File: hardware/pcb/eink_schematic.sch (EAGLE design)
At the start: 2 parts, among them U1 NUCLEUM

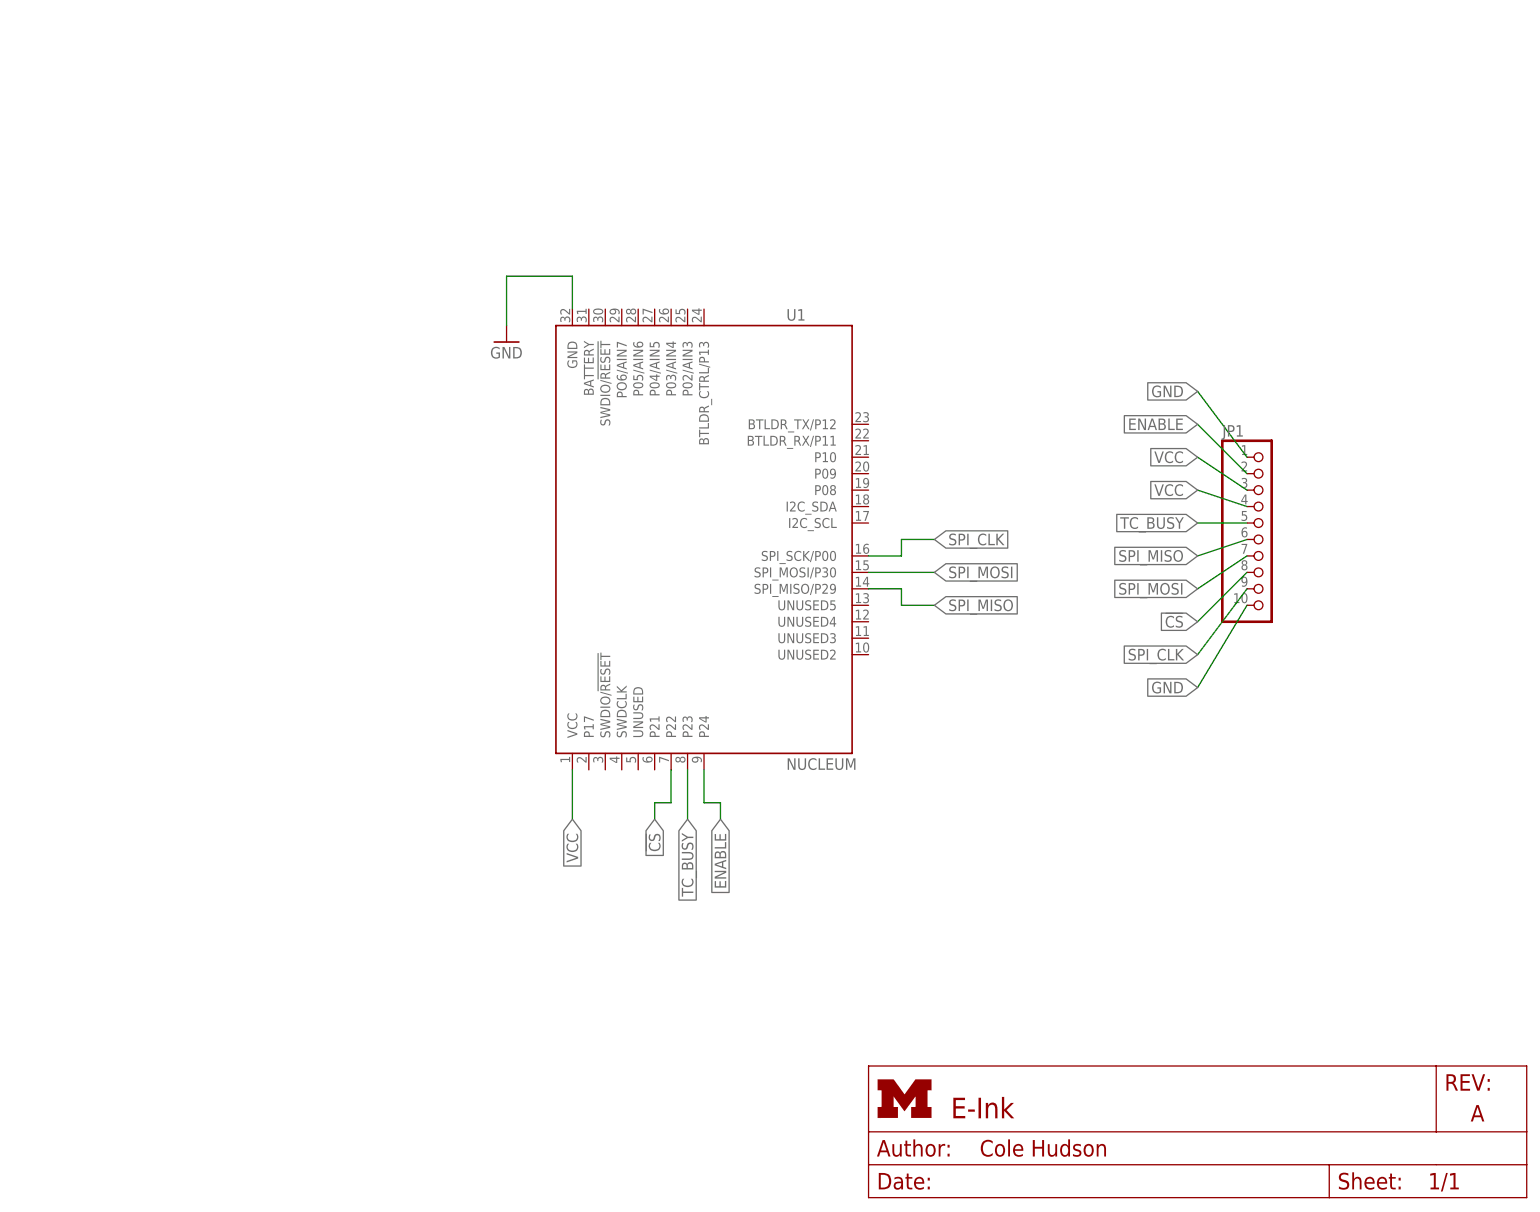
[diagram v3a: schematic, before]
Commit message: added buck/boost regulator to schematic
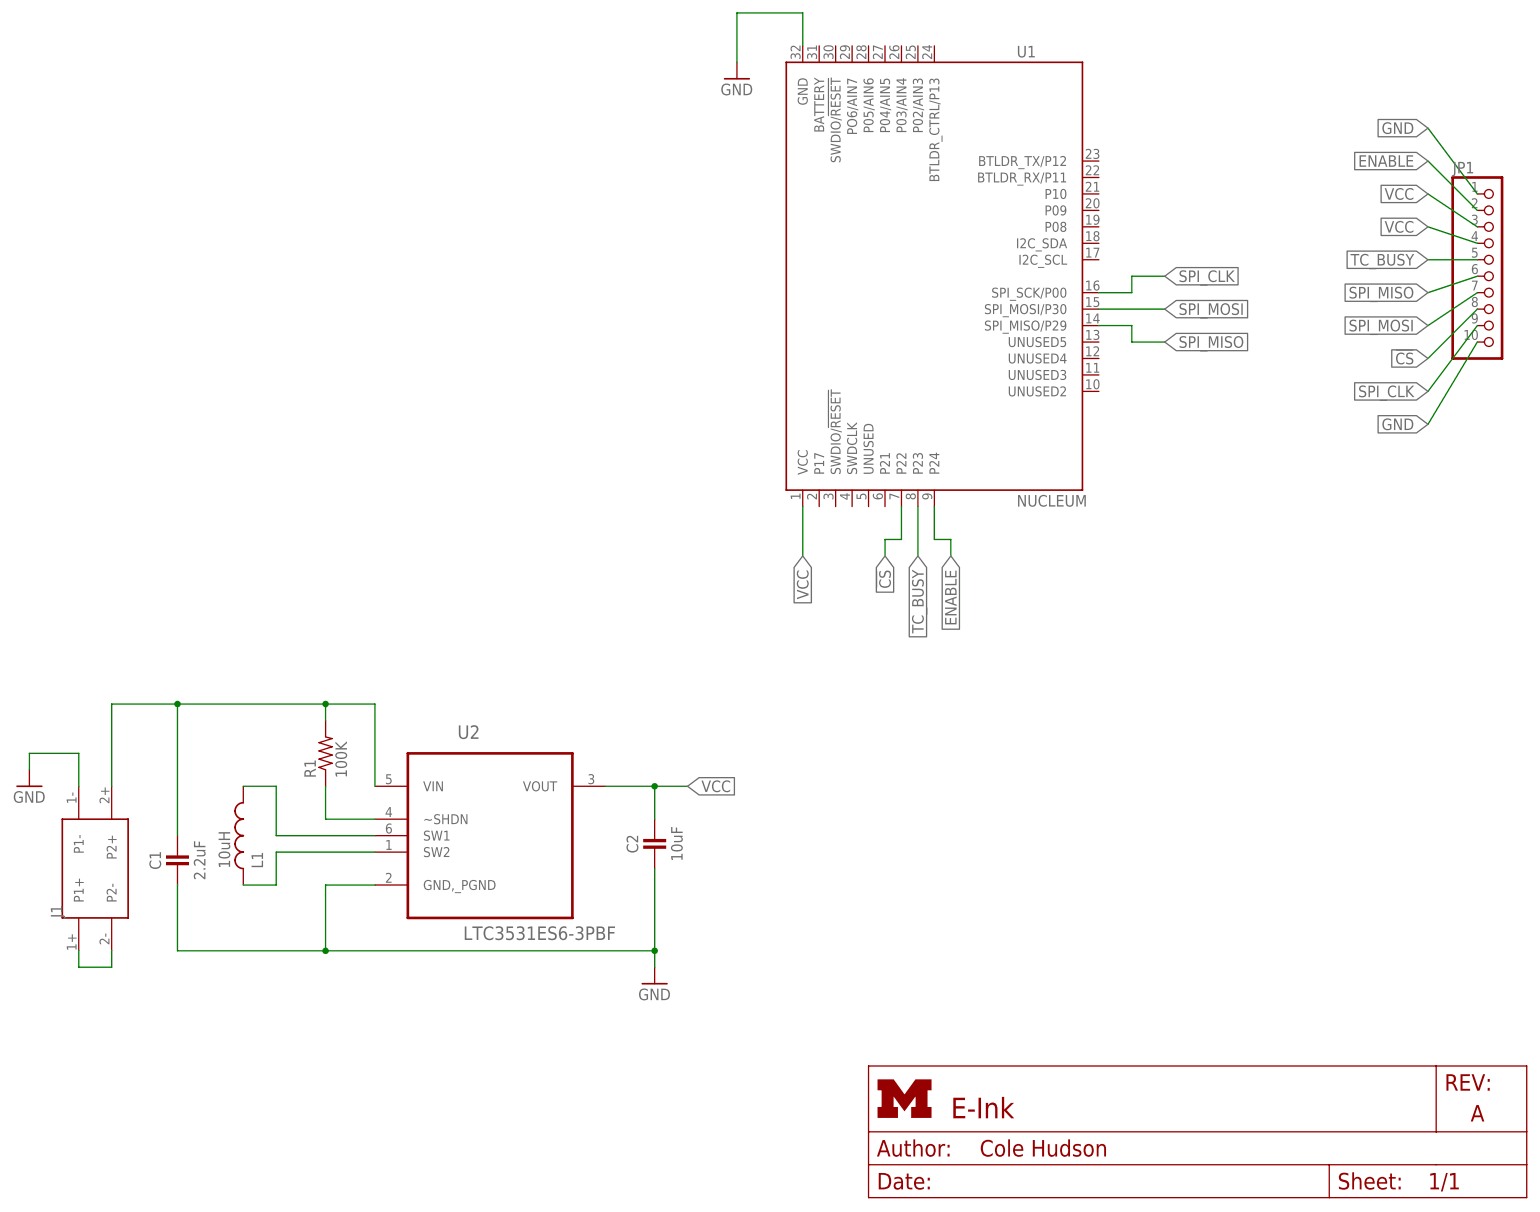
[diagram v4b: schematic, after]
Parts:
- added C1: 2.2uF, passives:CAPACITOR
- added C2: 10uF, passives:CAPACITOR
- added J1: AA_BAT_PACKSMD, connector:AA_BAT_PACKSMD
- added L1: 10uH, umich:L-US0207/10
- added R1: 100K, passives:RESISTOR
- added U2: LTC3531ES6-3PBF, LTC_By_element14_Batch_1:LTC3531ES6-3PBF
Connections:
- new net N$1: L1.1, U2.SW1
- new net N$2: L1.2, U2.SW2
- new net N$4: C1.1, J1.P2+, R1.2, U2.VIN
- new net N$5: J1.P1+, J1.P2-
- new net N$6: R1.1, U2.~SHDN
- net GND: now also C1.2, C2.2, J1.P1-, U2.GND,_PGND
- net VCC: now also C2.1, U2.VOUT
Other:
- moved on the sheet: JP1, U1

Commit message: Added some libs, buck/boost regulator, and barrel jack
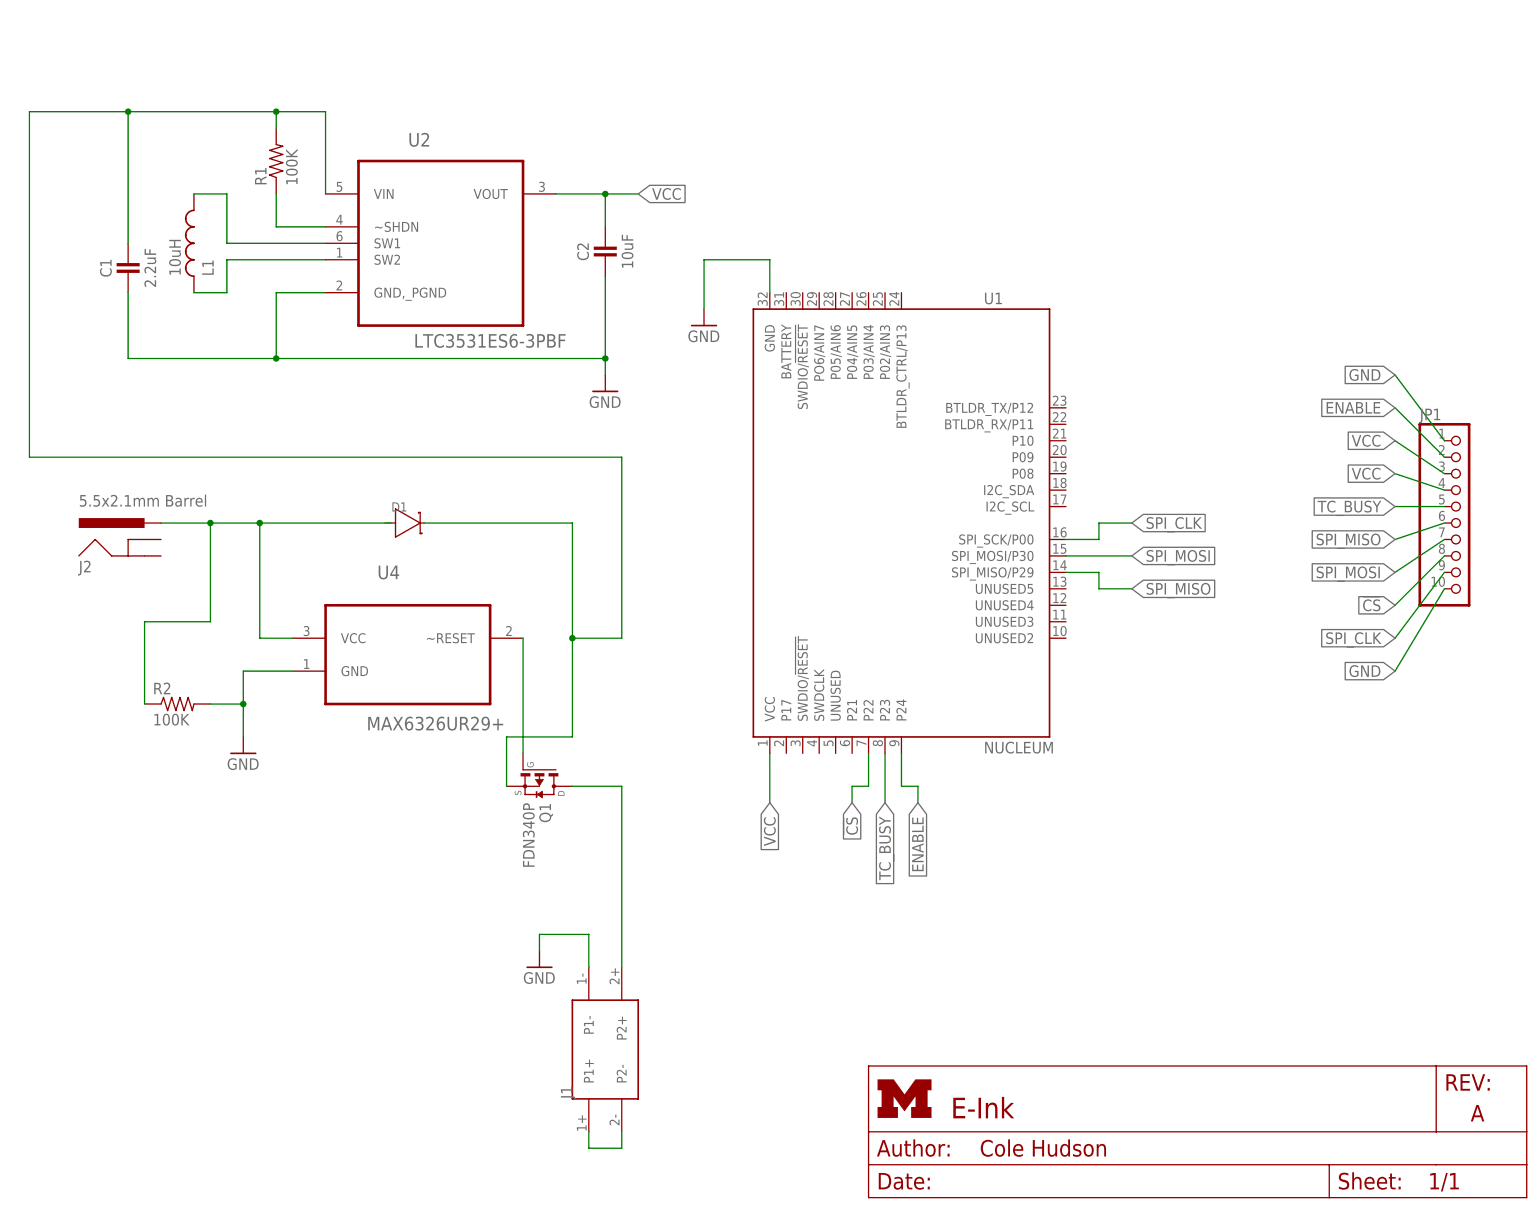
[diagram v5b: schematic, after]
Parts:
- added D1: (no value), nxp:DIODE[SCHOTKY]-SOD123W
- added J2: 5.5x2.1mm Barrel, SparkFun-Connectors:POWER_JACKSMD
- added Q1: FDN340P, transistor-fet:FDN340P
- added R2: 100K, passives:RESISTOR
- added U4: MAX6326UR29+, Maxim_By_element14_Batch_1:MAX6326UR29+
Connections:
- net N$1 renamed SW1
- net N$2 renamed SW2
- net N$6 renamed !SHDN
- new net N$1: Q1.G, U4.~RESET
- new net N$2: D1.1, J2.PWR, R2.1, U4.VCC
- new net N$3: C1.1, D1.2, Q1.S, R1.2, U2.VIN
- net GND: now also R2.2, U4.GND
- net N$4: now also Q1.D; no longer C1.1, R1.2, U2.VIN
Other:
- moved on the sheet: C1, C2, J1, JP1, L1, R1, U1, U2

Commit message: added digikey part numbers for everything
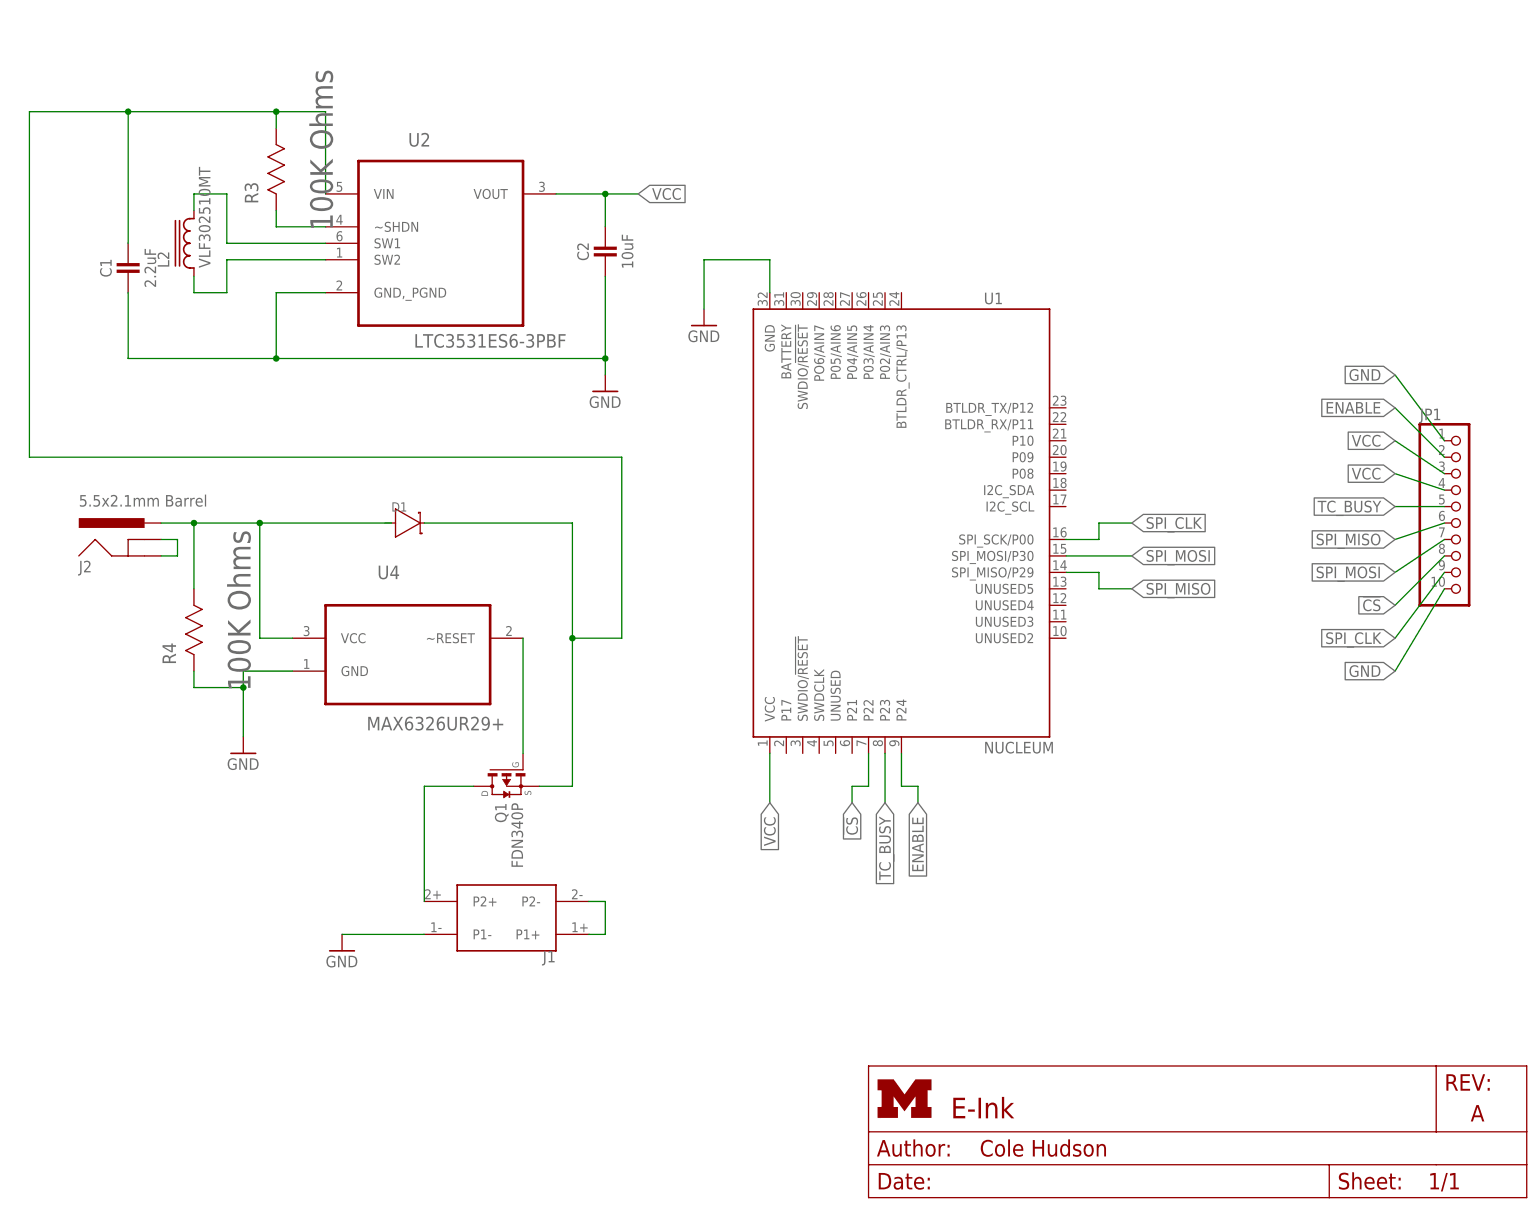
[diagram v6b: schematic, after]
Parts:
- removed L1: 10uH, umich:L-US0207/10
- removed R1, R2: 100K, passives:RESISTOR
- added L2: VLF302510MT, inductor-tdk:VLF302510MT
- added R3, R4: 100K Ohms, Yageo_By_element14_Batch_1:RC0603JR-07100KL
- C1: DIGIKEY (none) -> 490-3296-1-ND
- C2: DIGIKEY (none) -> 490-10693-1-ND
- D1: DIGIKEY (none) -> SS15FACT-ND
- J1: DIGIKEY (none) -> 36-1012-ND
- J2: DIGIKEY (none) -> CP-002AHPJCT-ND
- JP1: DIGIKEY (none) -> S5446-ND
- Q1: DIGIKEY (none) -> FDN340PCT-ND
- U2: DIGIKEY (none) -> LTC3531ES6-3.3#TRMPBFCT-ND
- U4: DIGIKEY (none) -> MAX6326UR29+TCT-ND
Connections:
- new net N$6: J2.GND, J2.GNDBREAK
- net !SHDN: now also R3.R2; no longer R1.1
- net GND: now also R4.R2; no longer R2.2
- net N$2: now also R4.R1; no longer R2.1
- net N$3: now also R3.R1; no longer R1.2
- net SW1: now also L2.2; no longer L1.1
- net SW2: now also L2.1; no longer L1.2
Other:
- moved on the sheet: J1, Q1

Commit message: Eagle: pretty sure I got things wired up
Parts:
- R4: DIGIKEY 311-100KGRCT-ND -> (none)
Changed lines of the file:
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@@
 <attribute name="DIGIKEY" value="311-100KGRCT-ND"/>
 </part>
-<part name="R4" library="Yageo_By_element14_Batch_1" deviceset="RC0603JR-07100KL" device="" value="100K Ohms">
-<attribute name="DIGIKEY" value="311-100KGRCT-ND"/>
-</part>
+<part name="R4" library="Yageo_By_element14_Batch_1" deviceset="RC0603JR-07100KL" device="" value="100K Ohms"/>
 </parts>
 <sheets>
@@
 <attribute name="DIGIKEY" x="55.88" y="152.4" size="1.778" layer="96" rot="R90" display="off"/>
 </instance>
-<instance part="R4" gate="A" x="43.18" y="81.28" rot="R90">
-<attribute name="DIGIKEY" x="43.18" y="81.28" size="1.778" layer="96" rot="R90" display="off"/>
-</instance>
+<instance part="R4" gate="A" x="43.18" y="81.28" rot="R90"/>
 </instances>
 <busses>
